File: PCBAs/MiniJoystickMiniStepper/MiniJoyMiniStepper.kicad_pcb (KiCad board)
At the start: 2 copper layers, 127 x 73.7 mm, 21 parts, among them J1 STEPPER_UNI_5P, J10 TH_0.1_1x1, J11 TH_0.1_1x1, J2 STEPPER_UNI_5P, J28 TH_0.1_1x1, J29 TH_0.1_1x1, J50 STEPPER_UNI_5P, J51 STEPPER_UNI_5P, J6 TH_0.1_1x1, J7 TH_0.1_1x1, J8 TH_0.1_1x1, J9 TH_0.1_1x1, U1 ADAFRUIT_FEATHER_M0, U2 ULN2803, U3 ULN2803

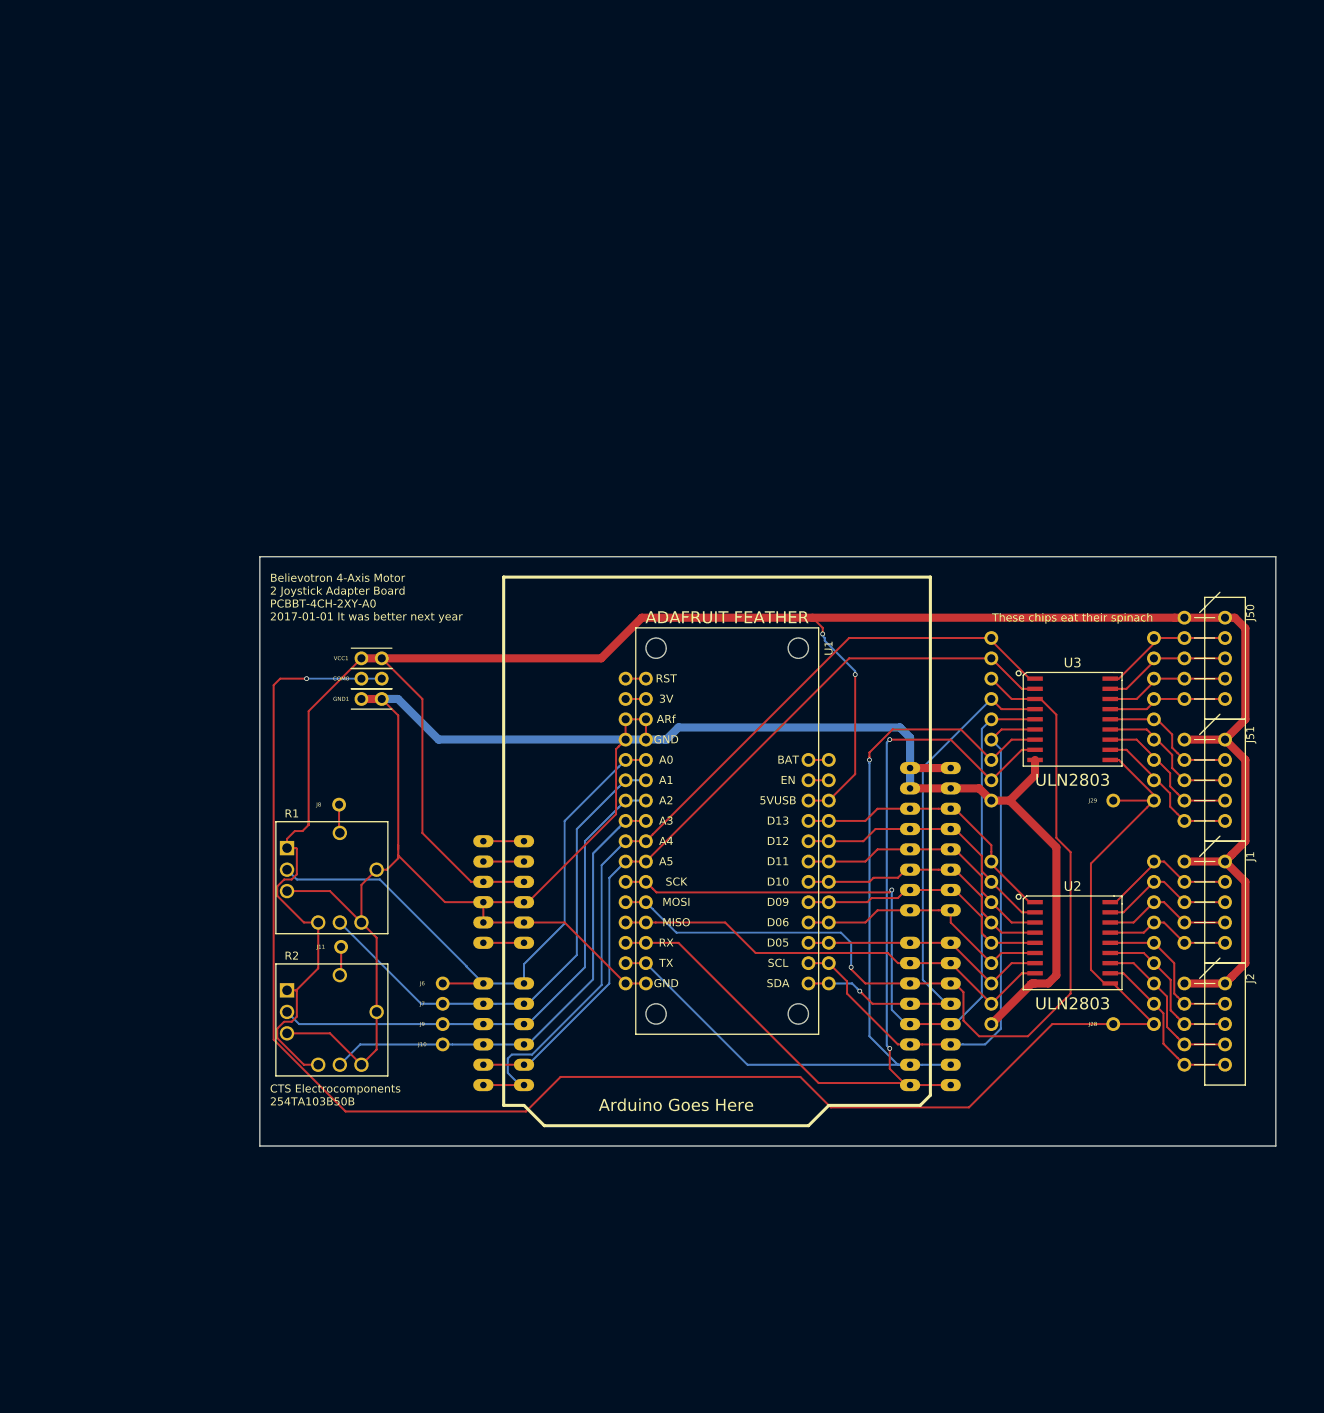
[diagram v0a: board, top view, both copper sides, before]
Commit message: Added ARM M0, Osc, Joystick, and other footprints/symbols
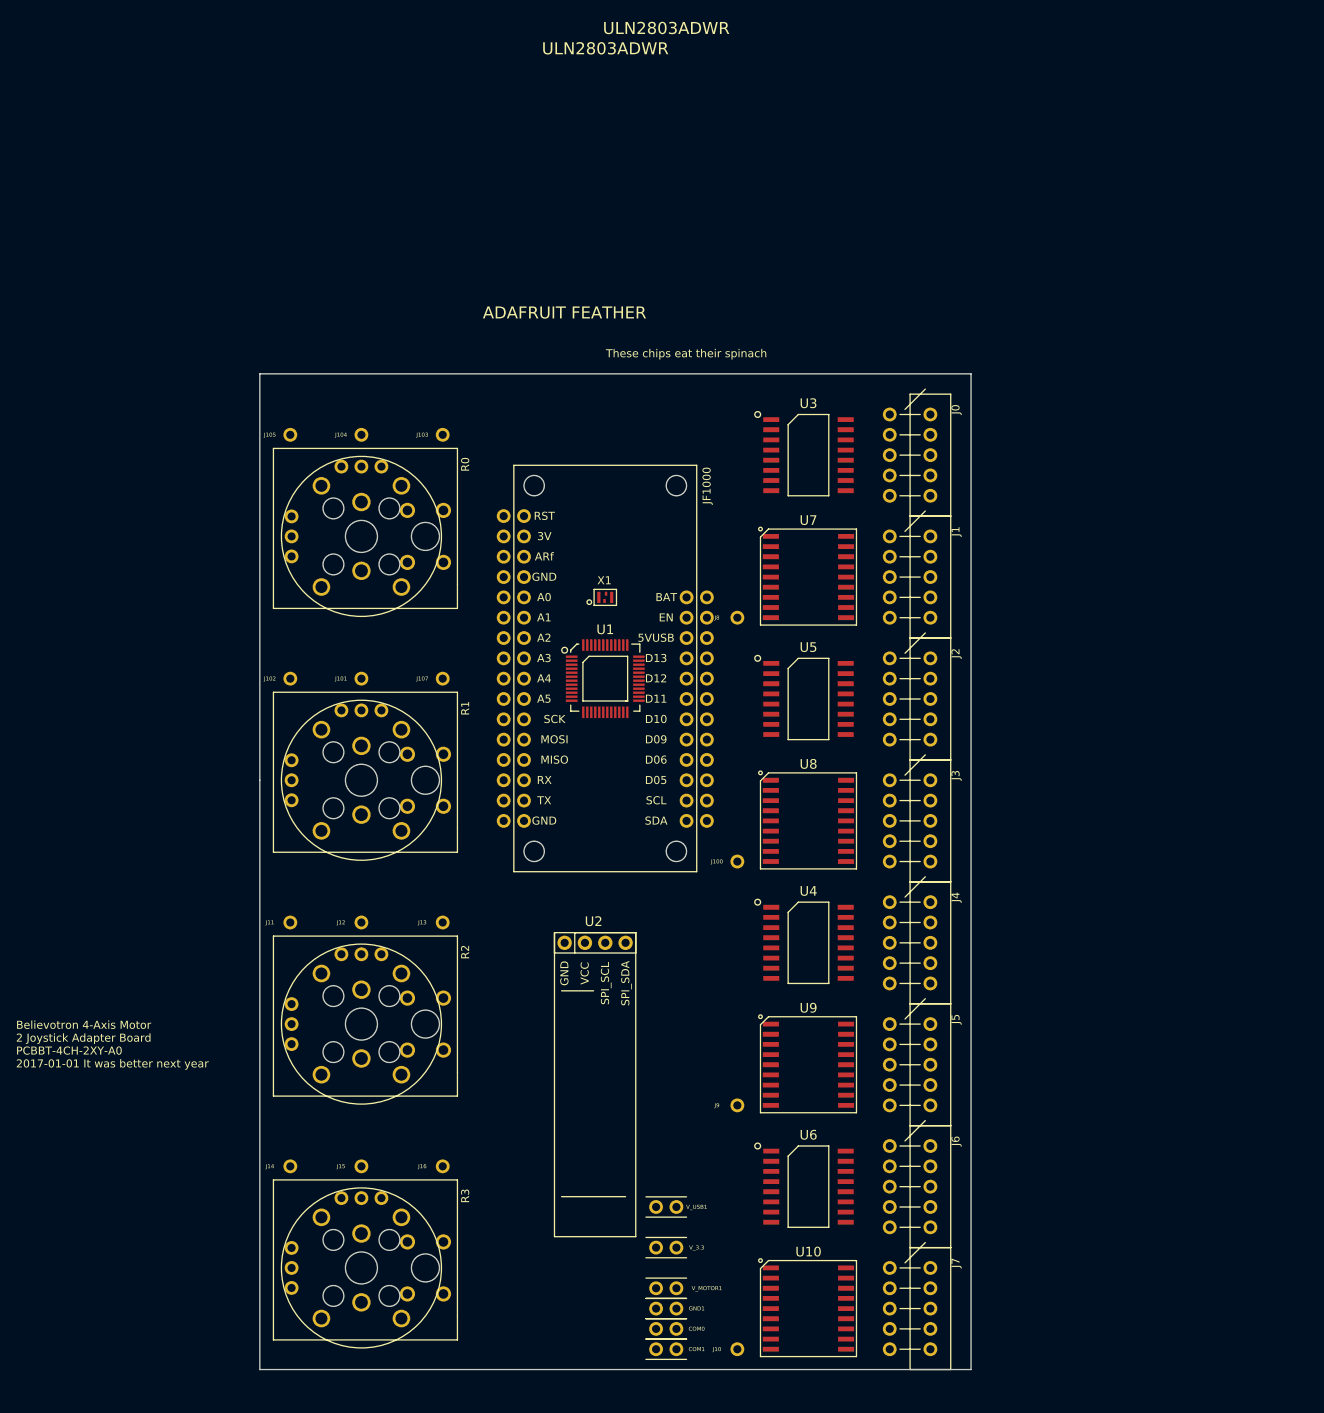
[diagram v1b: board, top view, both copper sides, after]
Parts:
- removed J28, J29: TH_0.1_1x1, Liberry:single_0.1
- removed J50, J51: STEPPER_UNI_5P, Liberry:M20-1060500_DEBUG
- removed SHIELD1: ARDUINO_SHIELD, Liberry:ARDUINO_SHIELD_2_debug
- removed VCC1: CONN_01X01, Liberry:TH_0.1_1x2_Jumper
- added COM1: CONN_01X01, Liberry:TH_0.1_1x2_Jumper, F.Cu at (153.7, 160.0)
- added J0: STEPPER_UNI_5P, Liberry:M20-1060500_DEBUG, F.Cu at (185.4, 48.3)
- added J100: TH_0.1_1x1, Liberry:single_0.1, F.Cu at (161.3, 99.1)
- added J101: TH_0.1_1x1, Liberry:single_0.1, F.Cu at (114.3, 76.2)
- added J102: TH_0.1_1x1, Liberry:single_0.1, F.Cu at (105.4, 76.2)
- added J103: TH_0.1_1x1, Liberry:single_0.1, F.Cu at (124.5, 45.7)
- added J104: TH_0.1_1x1, Liberry:single_0.1, F.Cu at (114.3, 45.7)
- added J105: TH_0.1_1x1, Liberry:single_0.1, F.Cu at (105.4, 45.7)
- added J107: TH_0.1_1x1, Liberry:single_0.1, F.Cu at (124.5, 76.2)
- added J12: TH_0.1_1x1, Liberry:single_0.1, F.Cu at (114.3, 106.7)
- added J13: TH_0.1_1x1, Liberry:single_0.1, F.Cu at (124.5, 106.7)
- added J14: TH_0.1_1x1, Liberry:single_0.1, F.Cu at (105.4, 137.2)
- added J15: TH_0.1_1x1, Liberry:single_0.1, F.Cu at (114.3, 137.2)
- added J16: TH_0.1_1x1, Liberry:single_0.1, F.Cu at (124.5, 137.2)
- added J3: STEPPER_UNI_5P, Liberry:M20-1060500_DEBUG, F.Cu at (185.4, 94.0)
- added J4: STEPPER_UNI_5P, Liberry:M20-1060500_DEBUG, F.Cu at (185.4, 109.2)
- added J5: STEPPER_UNI_5P, Liberry:M20-1060500_DEBUG, F.Cu at (185.4, 124.5)
- added JF1000: ADAFRUIT_FEATHER_M0, Liberry:ADAFRUIT_FEATHER_debug_1, F.Cu at (134.6, 94.0)
- added R0: XYJOY, MiniJoystickMiniStepper:JOY_ALPS_RKJXV1224005, F.Cu at (114.3, 58.4)
- added R3: XYJOY, MiniJoystickMiniStepper:JOY_ALPS_RKJXV1224005, F.Cu at (114.3, 149.9)
- added U10: ULN2803, MiniJoystickMiniStepper:SOIC-18_1.27_9.4, F.Cu at (170.2, 154.9)
- added U4: CD74HC595, MiniJoystickMiniStepper:SOIC-16_1.27x9.3, F.Cu at (170.2, 109.2)
- added U5: CD74HC595, MiniJoystickMiniStepper:SOIC-16_1.27x9.3, F.Cu at (170.2, 78.7)
- added U6: CD74HC595, MiniJoystickMiniStepper:SOIC-16_1.27x9.3, F.Cu at (170.2, 139.7)
- added U7: ULN2803, MiniJoystickMiniStepper:SOIC-18_1.27_9.4, F.Cu at (170.2, 63.5)
- added U8: ULN2803, MiniJoystickMiniStepper:SOIC-18_1.27_9.4, F.Cu at (170.2, 94.0)
- added U9: ULN2803, MiniJoystickMiniStepper:SOIC-18_1.27_9.4, F.Cu at (170.2, 124.5)
- added V_3.3: CONN_01X01, Liberry:TH_0.1_1x2_Jumper, F.Cu at (153.7, 147.3)
- added V_MOTOR1: CONN_01X01, Liberry:TH_0.1_1x2_Jumper, F.Cu at (153.7, 152.4)
- added V_USB1: CONN_01X01, Liberry:TH_0.1_1x2_Jumper, F.Cu at (153.7, 142.2)
- added X1: SIT1533_MEMS_OSC, MiniJoystickMiniStepper:SiTime1533, F.Cu at (144.8, 66.0)
- J6, J7: value TH_0.1_1x1 -> STEPPER_UNI_5P; footprint Liberry:single_0.1 -> Liberry:M20-1060500_DEBUG
- R1, R2: footprint Liberry:XY_JOY_254TA103B50B -> MiniJoystickMiniStepper:JOY_ALPS_RKJXV1224005
- U1: value ADAFRUIT_FEATHER_M0 -> ATSAMD21G18A; footprint Liberry:ADAFRUIT_FEATHER_debug_1 -> MiniJoystickMiniStepper:QFP_48_0.5_8
- U2: value ULN2803 -> OLED_128x32_I2C; footprint Liberry:SOIC-18_DEBUG -> MiniJoystickMiniStepper:OLED_128x32
- U3: value ULN2803 -> CD74HC595; footprint Liberry:SOIC-18_DEBUG -> MiniJoystickMiniStepper:SOIC-16_1.27x9.3
- moved COM0 90.3 mm to (153.7, 157.5), turned to 180 degrees
- moved GND1 85.8 mm to (153.7, 154.9), turned to 180 degrees
- moved J7 71.9 mm to (185.4, 154.9), turned to 270 degrees
- moved J6 66.0 mm to (185.4, 139.7), turned to 270 degrees
- moved U2 55.9 mm to (147.3, 109.2)
- moved J8 55.0 mm to (161.3, 68.6)
- moved J1 54.8 mm to (185.4, 63.5)
- moved J2 54.8 mm to (185.4, 78.7)
- moved J10 53.0 mm to (161.3, 160.0)
- moved U3 46.7 mm to (170.2, 48.3)
- moved U1 38.4 mm to (144.8, 76.2), turned to 0 degrees
- moved J9 38.2 mm to (161.3, 129.5)
- moved R1 11.5 mm to (114.3, 88.9), turned to 90 degrees
- moved J11 7.04 mm to (105.4, 106.7)
- moved R2 3.10 mm to (114.3, 119.4), turned to 90 degrees
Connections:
- J1 pad 1: VCC -> /MOTOR_POWER
- J10 pad 1: /JOY1_AXIS1 -> /COM
- J11 pad 1: /JOY1_SW -> /JOY2_AXIS0
- J2 pad 1: VCC -> /MOTOR_POWER
- J6 pad 1: /JOY0_AXIS0 -> /MOTOR_POWER
- J7 pad 1: /JOY0_AXIS1 -> /MOTOR_POWER
- J8 pad 1: /JOY0_SW -> /COM
- J9 pad 1: /JOY1_AXIS0 -> /COM
- U2 pad 1: /M0_C0 -> Net-(U2-Pad1)
- U2 pad 2: /M0_C1 -> Net-(U2-Pad2)
- U2 pad 3: /M0_C2 -> Net-(U2-Pad3)
- U2 pad 4: /M0_C3 -> Net-(U2-Pad4)
- U3 pad 1: /M2_C0 -> Net-(U3-Pad1)
- U3 pad 10: /COM -> /!SCLR
- U3 pad 11: Net-(J51-Pad5) -> /CLK_DATA
- U3 pad 13: Net-(J51-Pad3) -> /!OE
- U3 pad 14: Net-(J51-Pad2) -> /DATA
- U3 pad 16: Net-(J50-Pad4) -> VCC
- U3 pad 2: /M2_C1 -> Net-(U3-Pad2)
- U3 pad 3: /M2_C2 -> Net-(U3-Pad3)
- U3 pad 4: /M2_C3 -> Net-(U3-Pad4)
- U3 pad 5: /M3_C0 -> Net-(U3-Pad5)
- U3 pad 6: /M3_C1 -> Net-(U3-Pad6)
- U3 pad 7: /M3_C2 -> Net-(U3-Pad7)
- U3 pad 8: /M3_C3 -> GND
- U3 pad 9: GND -> Net-(U3-Pad9)
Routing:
- net VCC: track 314.9 -> 0.00 mm, vias 2 -> 0
- net GND: track 290.5 -> 0.00 mm
- net /COM: track 227.5 -> 0.00 mm, vias 1 -> 0
- net /M3_C3: track 114.7 -> 0.00 mm, vias 2 -> 0
- net /M2_C2: track 114.4 -> 0.00 mm, vias 1 -> 0
- net /M3_C2: track 112.4 -> 0.00 mm, vias 1 -> 0
- net /M2_C0: track 108.3 -> 0.00 mm
- net /M3_C0: track 103.0 -> 0.00 mm, vias 1 -> 0
- net /M2_C1: track 99.3 -> 0.00 mm
- net /JOY0_AXIS0: track 76.4 -> 0.00 mm
- net /M3_C1: track 72.6 -> 0.00 mm
- net /M2_C3: track 68.2 -> 0.00 mm, vias 1 -> 0
- net /JOY1_AXIS0: track 66.8 -> 0.00 mm
- net /JOY0_AXIS1: track 63.3 -> 0.00 mm
- net /JOY1_AXIS1: track 60.6 -> 0.00 mm
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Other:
- board size 127 x 73.7 mm -> 88.9 x 124.5 mm
- board text added: "ULN2803ADWR"
- board text removed: "Arduino Goes Here"
- board text removed: "CTS Electrocomponents 254TA103B50B"
- board text removed: "ULN2803"

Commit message: 90% PCB placement
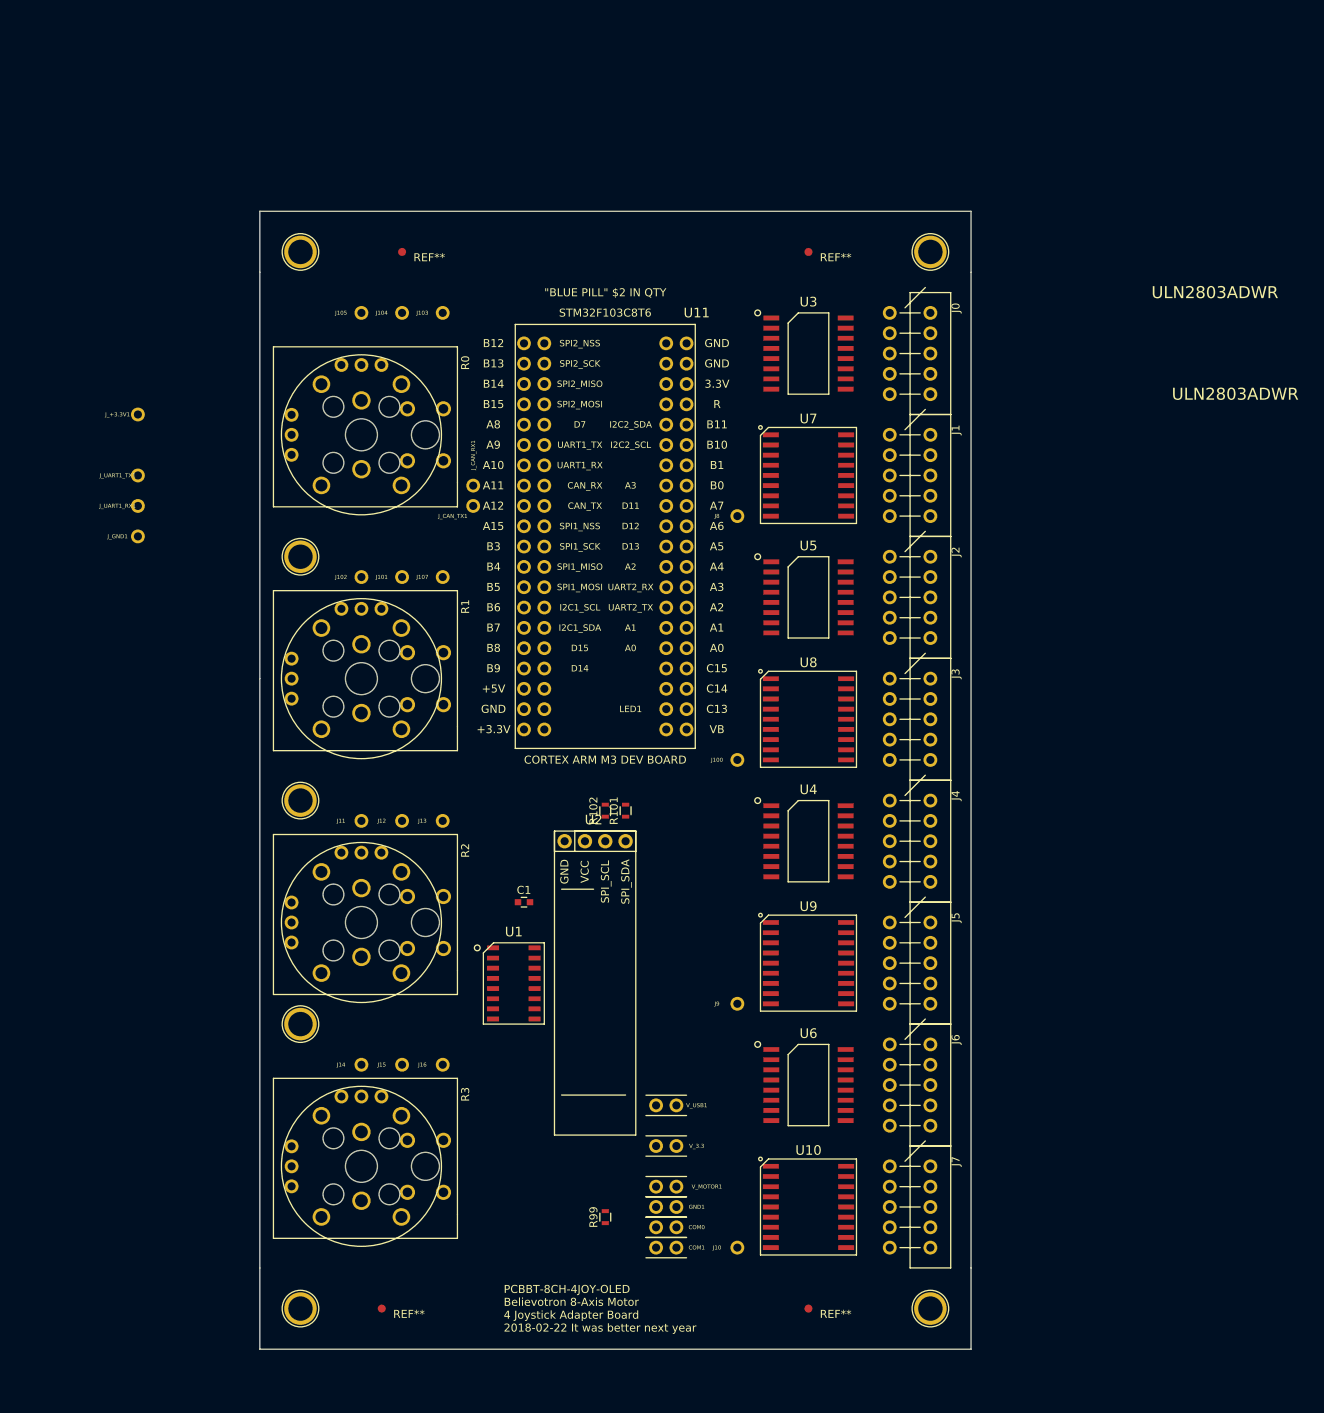
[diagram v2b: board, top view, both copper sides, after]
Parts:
- removed JF1000: ADAFRUIT_FEATHER_M0, Liberry:ADAFRUIT_FEATHER_debug_1
- removed X1: SIT1533_MEMS_OSC, MiniJoystickMiniStepper:SiTime1533
- added C1: 0.1 uF, Capacitors_SMD:C_0603, F.Cu at (134.6, 104.1)
- added J_+3.3V1: TH_0.1_1x1, Liberry:single_0.1, F.Cu at (86.4, 43.2)
- added J_CAN_RX1: TH_0.1_1x1, Liberry:single_0.1, F.Cu at (128.3, 52.1)
- added J_CAN_TX1: TH_0.1_1x1, Liberry:single_0.1, F.Cu at (128.3, 54.6)
- added J_GND1: TH_0.1_1x1, Liberry:single_0.1, F.Cu at (86.4, 58.4)
- added J_UART1_RX1: TH_0.1_1x1, Liberry:single_0.1, F.Cu at (86.4, 54.6)
- added J_UART1_TX1: TH_0.1_1x1, Liberry:single_0.1, F.Cu at (86.4, 50.8)
- added R101: 10K, Resistors_SMD:R_0603, F.Cu at (147.3, 92.7)
- added R102: 10K, Resistors_SMD:R_0603, F.Cu at (144.8, 92.7)
- added R99: 0, Resistors_SMD:R_0603, F.Cu at (144.8, 143.5)
- added REF**: Fiducial_1mm_Dia_2.54mm_Outer_CopperTop, Fiducials:Fiducial_1mm_Dia_2.54mm_Outer_CopperTop, F.Cu at (119.4, 22.9)
- added REF**: 1pin, Connect:1pin, F.Cu at (106.7, 22.9)
- added REF**: Fiducial_1mm_Dia_2.54mm_Outer_CopperTop, Fiducials:Fiducial_1mm_Dia_2.54mm_Outer_CopperTop, F.Cu at (170.2, 22.9)
- added REF**: Fiducial_1mm_Dia_2.54mm_Outer_CopperTop, Fiducials:Fiducial_1mm_Dia_2.54mm_Outer_CopperTop, F.Cu at (116.8, 154.9)
- added REF**: Fiducial_1mm_Dia_2.54mm_Outer_CopperTop, Fiducials:Fiducial_1mm_Dia_2.54mm_Outer_CopperTop, F.Cu at (170.2, 154.9)
- added REF**: 1pin, Connect:1pin, F.Cu at (106.7, 154.9)
- added REF**: 1pin, Connect:1pin, F.Cu at (185.4, 154.9)
- added REF**: 1pin, Connect:1pin, F.Cu at (185.4, 22.9)
- added REF**: 1pin, Connect:1pin, F.Cu at (106.7, 119.4)
- added REF**: 1pin, Connect:1pin, F.Cu at (106.7, 91.4)
- added REF**: 1pin, Connect:1pin, F.Cu at (106.7, 61.0)
- added U11: STM32F103C8T6_BLUE_PILL, MiniJoystickMiniStepper:BLUEPILL_CORTEXM3_STM32F103C8T6, F.Cu at (144.8, 58.4)
- U1: value ATSAMD21G18A -> MCP3008T-I/SL; footprint MiniJoystickMiniStepper:QFP_48_0.5_8 -> MiniJoystickMiniStepper:SOIC-16
- moved U1 39.8 mm to (133.3, 114.3), turned to 270 degrees
- moved J105 17.6 mm to (114.3, 30.5)
- moved J104 16.1 mm to (119.4, 30.5)
- moved J102 15.5 mm to (114.3, 63.5)
- moved J11 15.5 mm to (114.3, 94.0)
- moved J14 15.5 mm to (114.3, 124.5)
- moved J103 15.2 mm to (124.5, 30.5)
- moved J101 13.7 mm to (119.4, 63.5)
- moved J12 13.7 mm to (119.4, 94.0)
- moved J15 13.7 mm to (119.4, 124.5)
- moved COM1 12.7 mm to (153.7, 147.3)
- moved J10 12.7 mm to (161.3, 147.3)
- moved R3 12.7 mm to (114.3, 137.2)
- moved V_MOTOR1 12.7 mm to (153.7, 139.7)
- moved V_USB1 12.7 mm to (153.7, 129.5)
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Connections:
- net /!OE renamed /!MOTOR_OE
- net /!SCLR renamed /!MOTOR_SCLR
- net /CLK_DATA renamed /MOTOR_CLK_DATA
- net Net-(U3-Pad12) renamed /MOTOR_CLK_OUT
- U1 pad 1: Net-(U1-Pad1) -> /JOY0_AXIS0
- U1 pad 10: Net-(U1-Pad10) -> /SPI1_CS
- U1 pad 11: Net-(U1-Pad11) -> /SPI1_MOSI
- U1 pad 12: Net-(U1-Pad12) -> /SPI1_MISO
- U1 pad 13: Net-(U1-Pad13) -> /SPI1_SCK
- U1 pad 14: Net-(U1-Pad14) -> GND
- U1 pad 15: Net-(U1-Pad15) -> +3V3
- U1 pad 16: Net-(U1-Pad16) -> +3V3
- U1 pad 2: Net-(U1-Pad2) -> /JOY0_AXIS1
- U1 pad 4: Net-(U1-Pad4) -> /JOY1_AXIS1
- U1 pad 5: Net-(U1-Pad5) -> /JOY2_AXIS0
- U1 pad 6: Net-(U1-Pad6) -> /JOY2_AXIS1
- U1 pad 7: Net-(U1-Pad7) -> /JOY3_AXIS0
- U1 pad 8: Net-(U1-Pad8) -> /JOY3_AXIS1
- U1 pad 9: Net-(U1-Pad9) -> GND
- U2 pad 1: Net-(U2-Pad1) -> GND
- U2 pad 2: Net-(U2-Pad2) -> +3V3
- U2 pad 3: Net-(U2-Pad3) -> /I2C1_SCL
- U2 pad 4: Net-(U2-Pad4) -> /I2C1_SDA
- U3 pad 14: /DATA -> /MOTOR_DATA
- U3 pad 16: VCC -> +3V3
- U4 pad 16: VCC -> +3V3
- U5 pad 16: VCC -> +3V3
- U6 pad 16: VCC -> +3V3
- V_3.3 pad 1: VCC -> +3V3
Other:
- board size 88.9 x 124.5 mm -> 88.9 x 142.2 mm
- board text added: "PCBBT-8CH-4JOY-OLED Believotron 8-Axis Motor 4 Joystick Adapter Board 2018-02-22 It was better next year"
- board text removed: "ADAFRUIT FEATHER"
- board text removed: "Believotron 4-Axis Motor 2 Joystick Adapter Board PCBBT-4CH-2XY-A0 2017-01-01 It was better next year"
- board text removed: "These chips eat their spinach"
